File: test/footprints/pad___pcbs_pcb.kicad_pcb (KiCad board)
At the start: 2 copper layers, 4 parts

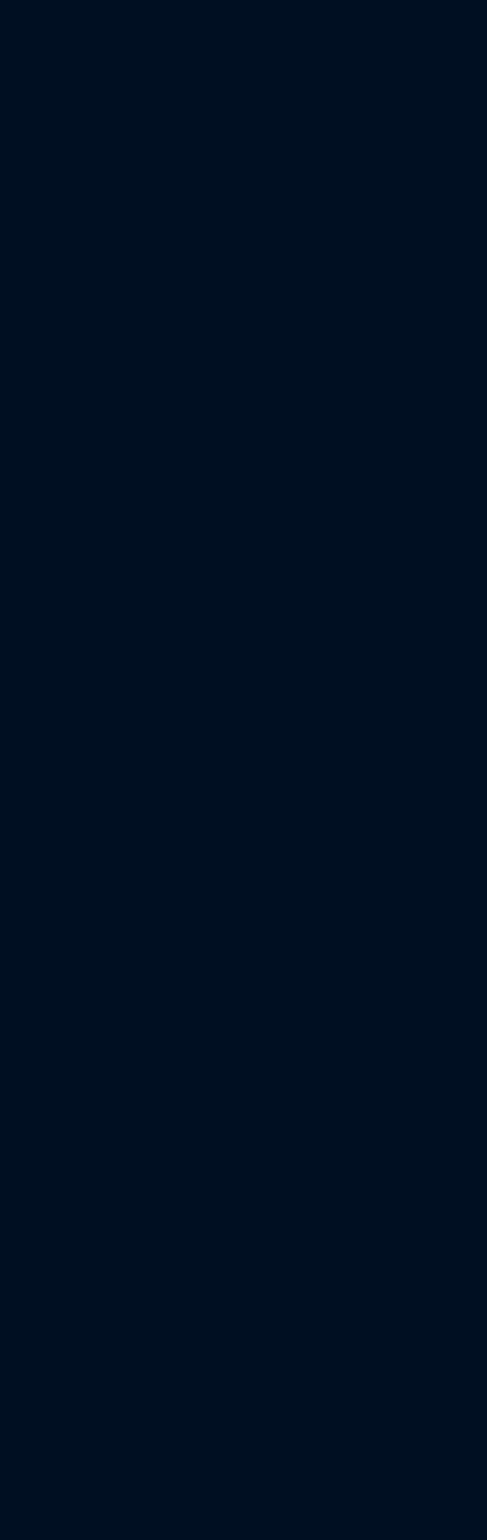
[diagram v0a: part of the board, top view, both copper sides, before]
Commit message: expand code coverage for `pad` footprint
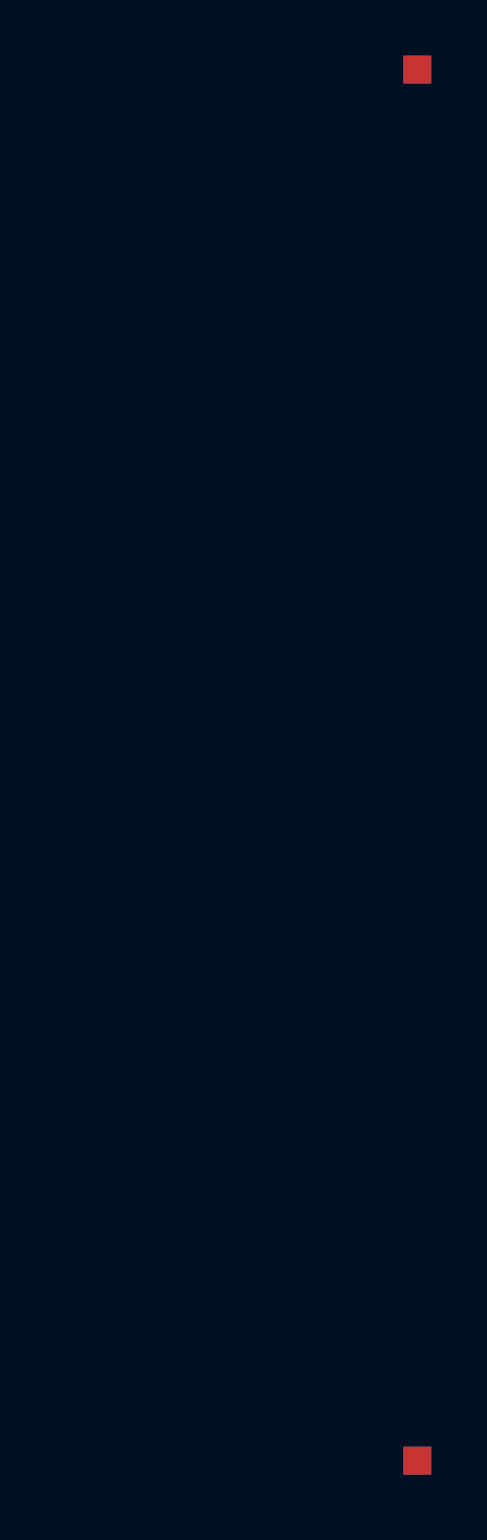
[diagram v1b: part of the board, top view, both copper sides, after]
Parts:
- added PAD5: , SMDPad, F.Cu at (100.0, 0.00)
- added PAD6: , SMDPad, F.Cu at (100.0, -50.0)
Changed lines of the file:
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@@
+            (pad 1 smd rect (at 0 0 0) (size 1 1) (layers B.Cu B.Paste B.Mask) (net 1 "net"))
+        )
+        (module SMDPad (layer F.Cu)
+            (at 100 0 0)
+            (fp_text reference "PAD5" (at 0 0) (layer F.SilkS) hide (effects (font (size 1.27 1.27) (thickness 0.15))))
+            (fp_text value "" (at 0 0) (layer F.SilkS) hide (effects (font (size 1.27 1.27) (thickness 0.15))))
+            (pad 1 smd rect (at 0 0 0) (size 1 1) (layers F.Cu F.Paste F.Mask) (net 1 "net"))
+            (pad 1 smd rect (at 0 0 0) (size 1 1) (layers B.Cu B.Paste B.Mask) (net 1 "net"))
+        )
+        (module SMDPad (layer F.Cu)
+            (at 100 -50 0)
+            (fp_text reference "PAD6" (at 0 0) (layer F.SilkS) hide (effects (font (size 1.27 1.27) (thickness 0.15))))
+            (fp_text value "" (at 0 0) (layer F.SilkS) hide (effects (font (size 1.27 1.27) (thickness 0.15))))
+            (pad 1 smd rect (at 0 0 0) (size 1 1) (layers F.Cu F.Paste F.Mask) (net 1 "net"))
             (pad 1 smd rect (at 0 0 0) (size 1 1) (layers B.Cu B.Paste B.Mask) (net 1 "net"))
         )
